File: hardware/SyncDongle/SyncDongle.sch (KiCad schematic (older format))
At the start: 3 parts

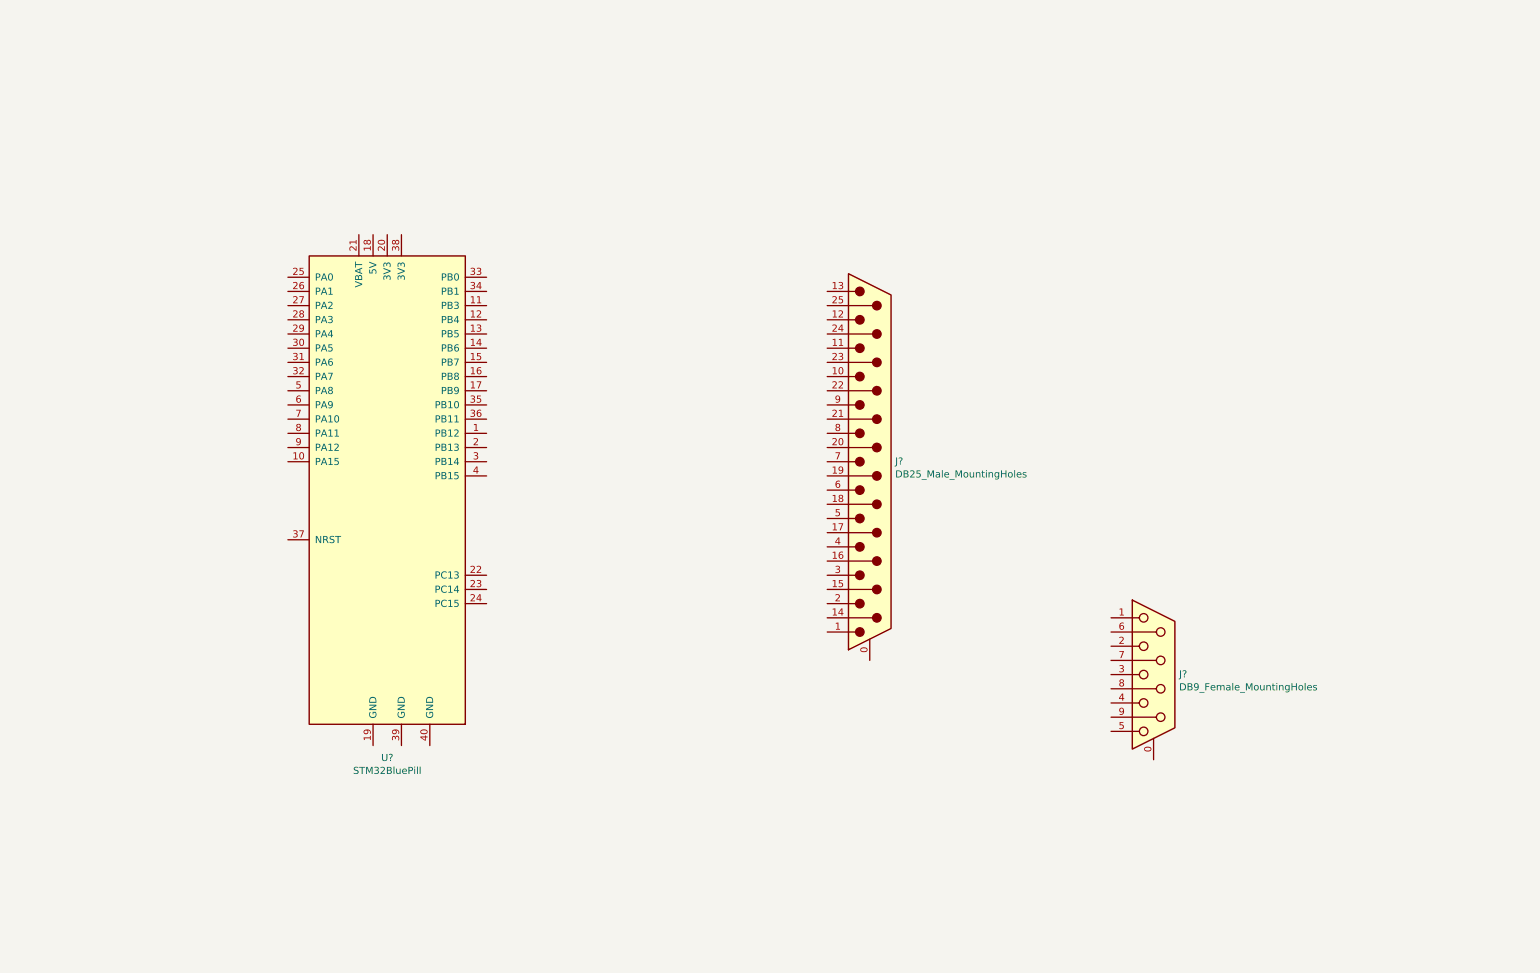
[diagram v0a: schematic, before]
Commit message: Added MAX208
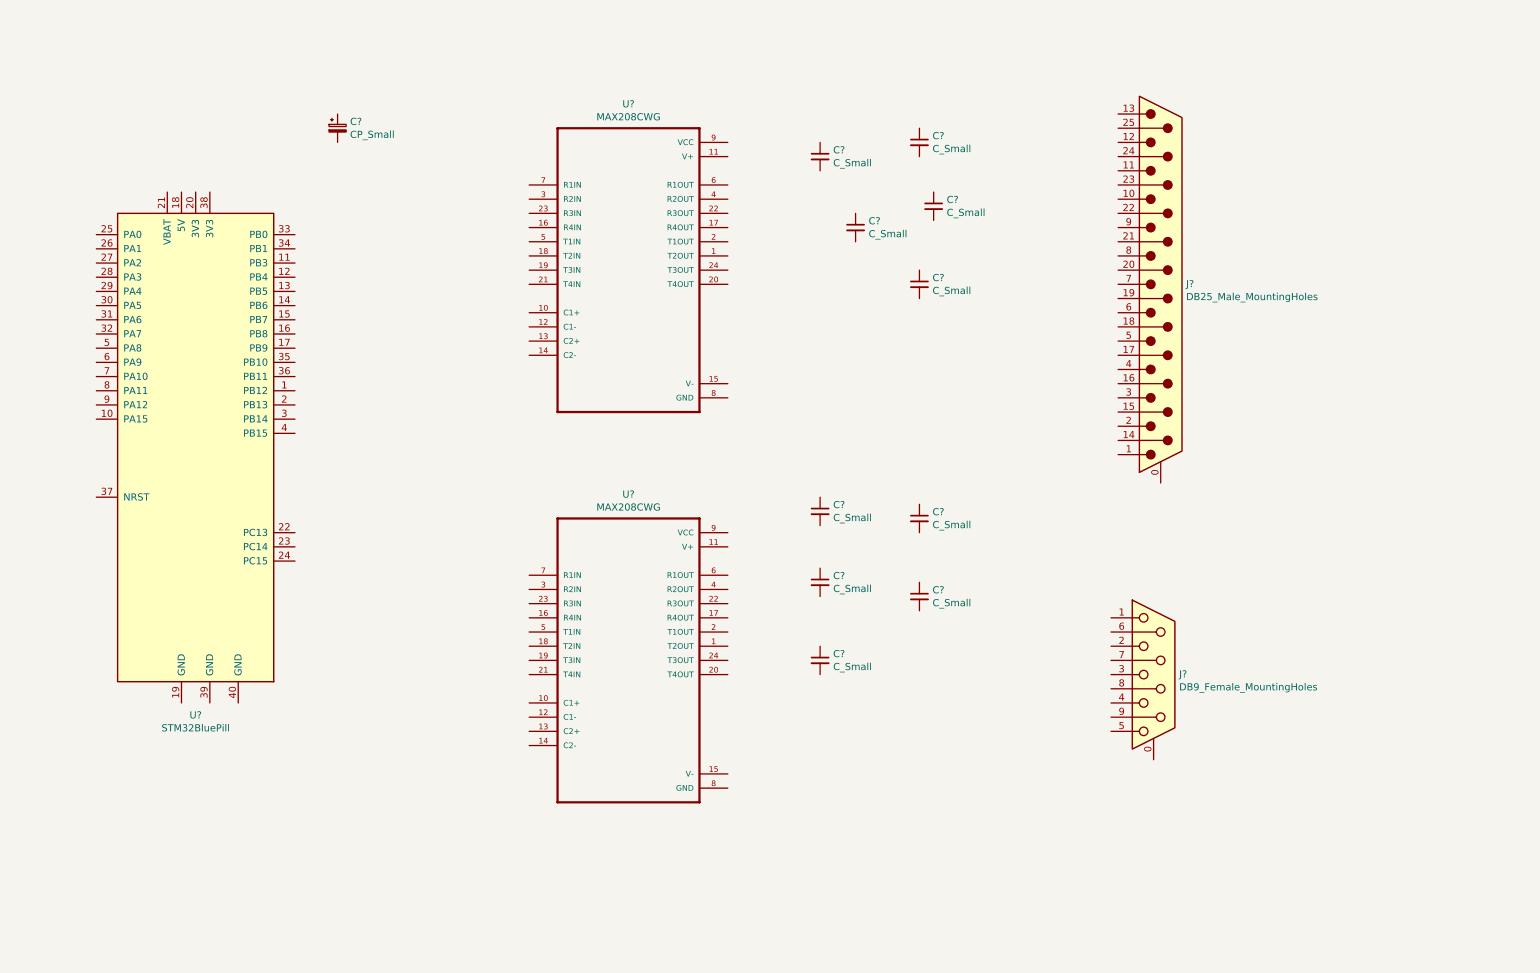
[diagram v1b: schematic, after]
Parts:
- added C? (x10): C_Small, symbol Device:C_Small
- added C?: CP_Small, symbol Device:CP_Small
- added U? (x2): MAX208CWG, SOIC127P1032X265-24N, symbol MAX208CWG:MAX208CWG
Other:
- moved on the sheet: J?, U?
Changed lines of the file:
@@
 EESchema Schematic File Version 4
+LIBS:SyncDongle-cache
 EELAYER 26 0
 EELAYER END
@@
 L MyLibrary:STM32BluePill U?
 U 1 1 5F1ADFA5
-P 3850 4050
-F 0 "U?" H 3850 2164 50  0000 C CNN
-F 1 "STM32BluePill" H 3850 2073 50  0000 C CNN
-F 2 "Housings_DIP:DIP-40_W15.24mm" H 3900 4150 50  0001 C CIN
-F 3 "" H 3850 4100 50  0001 C CNN
-	1    3850 4050
+P 2500 3750
+F 0 "U?" H 2500 1864 50  0000 C CNN
+F 1 "STM32BluePill" H 2500 1773 50  0000 C CNN
+F 2 "Housings_DIP:DIP-40_W15.24mm" H 2550 3850 50  0001 C CIN
+F 3 "" H 2500 3800 50  0001 C CNN
+	1    2500 3750
 	1    0    0    -1
 $EndComp
@@
 L Connector:DB25_Male_MountingHoles J?
 U 1 1 5F1AE32F
-P 7250 3850
-F 0 "J?" H 7429 3853 50  0000 L CNN
-F 1 "DB25_Male_MountingHoles" H 7429 3762 50  0000 L CNN
-F 2 "" H 7250 3850 50  0001 C CNN
-F 3 " ~" H 7250 3850 50  0001 C CNN
-	1    7250 3850
+P 9300 2600
+F 0 "J?" H 9479 2603 50  0000 L CNN
+F 1 "DB25_Male_MountingHoles" H 9479 2512 50  0000 L CNN
+F 2 "" H 9300 2600 50  0001 C CNN
+F 3 " ~" H 9300 2600 50  0001 C CNN
+	1    9300 2600
 	1    0    0    -1
 $EndComp
@@
 	1    0    0    -1
 $EndComp
+$Comp
+L MAX208CWG:MAX208CWG U?
+U 1 1 5F185462
+P 5550 2500
+F 0 "U?" H 5550 3670 50  0000 C CNN
+F 1 "MAX208CWG" H 5550 3579 50  0000 C CNN
+F 2 "SOIC127P1032X265-24N" H 5550 2500 50  0001 L BNN
+F 3 "SOIC-24 Maxim" H 5550 2500 50  0001 L BNN
+F 4 "Maxim Integrated" H 5550 2500 50  0001 L BNN "Field4"
+F 5 "MAX208CWG+" H 5550 2500 50  0001 L BNN "Field5"
+F 6 "https://snapeda.com/shop?store=DigiKey&id=128491" H 5550 2500 50  0001 L BNN "Field6"
+F 7 "4/4 Transceiver Full RS232 24-SOIC" H 5550 2500 50  0001 L BNN "Field7"
+F 8 "MAX208CWG+TTR-ND" H 5550 2500 50  0001 L BNN "Field8"
+F 9 "https://snapeda.com/shop?store=Mouser&id=128491" H 5550 2500 50  0001 L BNN "Field9"
+	1    5550 2500
+	1    0    0    -1
+$EndComp
+$Comp
+L MAX208CWG:MAX208CWG U?
+U 1 1 5F185592
+P 5550 5250
+F 0 "U?" H 5550 6420 50  0000 C CNN
+F 1 "MAX208CWG" H 5550 6329 50  0000 C CNN
+F 2 "SOIC127P1032X265-24N" H 5550 5250 50  0001 L BNN
+F 3 "SOIC-24 Maxim" H 5550 5250 50  0001 L BNN
+F 4 "Maxim Integrated" H 5550 5250 50  0001 L BNN "Field4"
+F 5 "MAX208CWG+" H 5550 5250 50  0001 L BNN "Field5"
+F 6 "https://snapeda.com/shop?store=DigiKey&id=128491" H 5550 5250 50  0001 L BNN "Field6"
+F 7 "4/4 Transceiver Full RS232 24-SOIC" H 5550 5250 50  0001 L BNN "Field7"
+F 8 "MAX208CWG+TTR-ND" H 5550 5250 50  0001 L BNN "Field8"
+F 9 "https://snapeda.com/shop?store=Mouser&id=128491" H 5550 5250 50  0001 L BNN "Field9"
+	1    5550 5250
+	1    0    0    -1
+$EndComp
+$Comp
+L Device:C_Small C?
+U 1 1 5F185808
+P 6900 1700
+F 0 "C?" H 6992 1746 50  0000 L CNN
+F 1 "C_Small" H 6992 1655 50  0000 L CNN
+F 2 "" H 6900 1700 50  0001 C CNN
+F 3 "~" H 6900 1700 50  0001 C CNN
+	1    6900 1700
+	1    0    0    -1
+$EndComp
+$Comp
+L Device:C_Small C?
+U 1 1 5F185866
+P 7600 1600
+F 0 "C?" H 7692 1646 50  0000 L CNN
+F 1 "C_Small" H 7692 1555 50  0000 L CNN
+F 2 "" H 7600 1600 50  0001 C CNN
+F 3 "~" H 7600 1600 50  0001 C CNN
+	1    7600 1600
+	1    0    0    -1
+$EndComp
+$Comp
+L Device:C_Small C?
+U 1 1 5F1858C6
+P 7700 2050
+F 0 "C?" H 7792 2096 50  0000 L CNN
+F 1 "C_Small" H 7792 2005 50  0000 L CNN
+F 2 "" H 7700 2050 50  0001 C CNN
+F 3 "~" H 7700 2050 50  0001 C CNN
+	1    7700 2050
+	1    0    0    -1
+$EndComp
+$Comp
+L Device:C_Small C?
+U 1 1 5F1858FA
+P 7150 2200
+F 0 "C?" H 7242 2246 50  0000 L CNN
+F 1 "C_Small" H 7242 2155 50  0000 L CNN
+F 2 "" H 7150 2200 50  0001 C CNN
+F 3 "~" H 7150 2200 50  0001 C CNN
+	1    7150 2200
+	1    0    0    -1
+$EndComp
+$Comp
+L Device:C_Small C?
+U 1 1 5F185938
+P 7600 2600
+F 0 "C?" H 7692 2646 50  0000 L CNN
+F 1 "C_Small" H 7692 2555 50  0000 L CNN
+F 2 "" H 7600 2600 50  0001 C CNN
+F 3 "~" H 7600 2600 50  0001 C CNN
+	1    7600 2600
+	1    0    0    -1
+$EndComp
+$Comp
+L Device:C_Small C?
+U 1 1 5F185976
+P 6900 4200
+F 0 "C?" H 6992 4246 50  0000 L CNN
+F 1 "C_Small" H 6992 4155 50  0000 L CNN
+F 2 "" H 6900 4200 50  0001 C CNN
+F 3 "~" H 6900 4200 50  0001 C CNN
+	1    6900 4200
+	1    0    0    -1
+$EndComp
+$Comp
+L Device:C_Small C?
+U 1 1 5F1859D8
+P 7600 4250
+F 0 "C?" H 7692 4296 50  0000 L CNN
+F 1 "C_Small" H 7692 4205 50  0000 L CNN
+F 2 "" H 7600 4250 50  0001 C CNN
+F 3 "~" H 7600 4250 50  0001 C CNN
+	1    7600 4250
+	1    0    0    -1
+$EndComp
+$Comp
+L Device:C_Small C?
+U 1 1 5F185A1C
+P 6900 4700
+F 0 "C?" H 6992 4746 50  0000 L CNN
+F 1 "C_Small" H 6992 4655 50  0000 L CNN
+F 2 "" H 6900 4700 50  0001 C CNN
+F 3 "~" H 6900 4700 50  0001 C CNN
+	1    6900 4700
+	1    0    0    -1
+$EndComp
+$Comp
+L Device:C_Small C?
+U 1 1 5F185A5C
+P 7600 4800
+F 0 "C?" H 7692 4846 50  0000 L CNN
+F 1 "C_Small" H 7692 4755 50  0000 L CNN
+F 2 "" H 7600 4800 50  0001 C CNN
+F 3 "~" H 7600 4800 50  0001 C CNN
+	1    7600 4800
+	1    0    0    -1
+$EndComp
+$Comp
+L Device:C_Small C?
+U 1 1 5F185AA2
+P 6900 5250
+F 0 "C?" H 6992 5296 50  0000 L CNN
+F 1 "C_Small" H 6992 5205 50  0000 L CNN
+F 2 "" H 6900 5250 50  0001 C CNN
+F 3 "~" H 6900 5250 50  0001 C CNN
+	1    6900 5250
+	1    0    0    -1
+$EndComp
+$Comp
+L Device:CP_Small C?
+U 1 1 5F185B27
+P 3500 1500
+F 0 "C?" H 3588 1546 50  0000 L CNN
+F 1 "CP_Small" H 3588 1455 50  0000 L CNN
+F 2 "" H 3500 1500 50  0001 C CNN
+F 3 "~" H 3500 1500 50  0001 C CNN
+	1    3500 1500
+	1    0    0    -1
+$EndComp

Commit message: Schematic almost ready.
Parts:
- removed C? (x5): C_Small, symbol Device:C_Small
- removed U?: MAX208CWG, SOIC127P1032X265-24N, symbol MAX208CWG:MAX208CWG
- added C10, C11, C4, C5, C9: 0.1u, symbol Device:C_Small
- added SW1: SW_DIP_x09, symbol Switch:SW_DIP_x09
- added U3: MAX208CWG, SOIC127P1032X265-24N, symbol MAX208CWG:MAX208CWG
- C1: renamed from C?; value CP_Small -> 10u
- C2, C3, C6, C7, C8: renamed from C?; value C_Small -> 0.1u
- gave numbers to parts that had none: 4
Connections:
- net labels added: +5V, CMOS_CKIN, CMOS_CKOUT, CMOS_CTS, CMOS_DCD, CMOS_DSR, CMOS_DTR, CMOS_D_RX, CMOS_D_TX, CMOS_RD, CMOS_RTS, CMOS_TD, EIA_CLK15, EIA_CLK17, EIA_CLK24, EIA_CLKIN, EIA_CTS, EIA_DCD, EIA_DSR, EIA_DTR, EIA_D_RX, EIA_D_TX, EIA_RD, EIA_RTS, EIA_TD, GND
- wire segments 0 -> 143
- no-connect marks 0 -> 51
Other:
- moved on the sheet: C1, C2, C3, C6, C7, C8, J1, J2, U2

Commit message: Fixed layout.
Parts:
- removed SW1: SW_DIP_x09, symbol Switch:SW_DIP_x09
- added SW1: SW_DIP_x10, Package_DIP:DIP-20_W7.62mm_LongPads, symbol Switch:SW_DIP_x10
- C1: footprint (none) -> Capacitor_THT:CP_Radial_D5.0mm_P2.00mm
- U2, U3: footprint SOIC127P1032X265-24N -> Package_DIP:DIP-24_W7.62mm_LongPads
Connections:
- net labels added: CMOS_RI, EIA_CLKOUT, EIA_RI
- net labels removed: EIA_CLK15, EIA_CLK17, EIA_CLK24
- wire segments 143 -> 150
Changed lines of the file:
@@
 F 0 "U2" H 5300 7220 50  0000 C CNN
 F 1 "MAX208CWG" H 5300 7129 50  0000 C CNN
-F 2 "SOIC127P1032X265-24N" H 5300 6050 50  0001 L BNN
+F 2 "Package_DIP:DIP-24_W7.62mm_LongPads" H 5300 6050 50  0001 L BNN
 F 3 "SOIC-24 Maxim" H 5300 6050 50  0001 L BNN
 F 4 "Maxim Integrated" H 5300 6050 50  0001 L BNN "Field4"
@@
 F 0 "C1" H 2738 1646 50  0000 L CNN
 F 1 "10u" H 2738 1555 50  0000 L CNN
-F 2 "" H 2650 1600 50  0001 C CNN
+F 2 "Capacitor_THT:CP_Radial_D5.0mm_P2.00mm" H 2650 1600 50  0001 C CNN
 F 3 "~" H 2650 1600 50  0001 C CNN
 	1    2650 1600
@@
 Text Label 4150 5850 0    50   ~ 0
 CMOS_D_TX
-Wire Wire Line
-	4600 5950 4500 5950
-Wire Wire Line
-	4600 6050 4500 6050
-Wire Wire Line
-	4600 6150 4500 6150
 Text Label 3600 6150 0    50   ~ 0
 CMOS_CKOUT
@@
 EIA_D_TX
 Wire Wire Line
-	6000 5950 6400 5950
-Text Label 6050 5950 0    50   ~ 0
-EIA_CLK24
-Wire Wire Line
 	6000 6050 6400 6050
-Text Label 6050 6050 0    50   ~ 0
-EIA_CLK17
 Wire Wire Line
 	6000 6150 6400 6150
 Text Label 6050 6150 0    50   ~ 0
-EIA_CLK15
+EIA_CLKOUT
 $Comp
 L power:GND #PWR05
@@
 Wire Wire Line
 	10250 3350 9750 3350
-$Comp
-L Switch:SW_DIP_x09 SW1
-U 1 1 5F1A85E1
-P 8550 2550
-F 0 "SW1" H 8550 3217 50  0000 C CNN
-F 1 "SW_DIP_x09" H 8550 3126 50  0000 C CNN
-F 2 "" H 8550 2550 50  0001 C CNN
-F 3 "" H 8550 2550 50  0001 C CNN
-	1    8550 2550
-	1    0    0    -1
-$EndComp
-Wire Wire Line
-	8850 2150 10250 2150
-Wire Wire Line
-	8850 2550 10250 2550
 Wire Wire Line
 	8850 2850 9100 2850
@@
 	10250 1450 9300 1450
 Wire Wire Line
-	9300 1450 9300 2250
-Wire Wire Line
-	9300 2250 9050 2250
-Wire Wire Line
-	8850 2350 9050 2350
-Wire Wire Line
-	9050 2350 9050 2250
-Connection ~ 9050 2250
-Wire Wire Line
-	9050 2250 8850 2250
-Wire Wire Line
-	8850 2450 9250 2450
-Wire Wire Line
-	9250 2450 9250 2750
+	9300 1450 9300 2050
+Wire Wire Line
+	9300 2050 9050 2050
+Wire Wire Line
+	8850 2150 9050 2150
+Wire Wire Line
+	9050 2150 9050 2050
+Connection ~ 9050 2050
+Wire Wire Line
+	9050 2050 8850 2050
+Wire Wire Line
+	8850 2550 9250 2550
+Wire Wire Line
+	9250 2550 9250 2750
 Wire Wire Line
 	9250 2750 10250 2750
 Wire Wire Line
-	8250 2150 7800 2150
-Wire Wire Line
-	8250 2250 8200 2250
-Wire Wire Line
-	8250 2350 7800 2350
-Wire Wire Line
-	8250 2450 7800 2450
-Wire Wire Line
-	8250 2550 7800 2550
+	8250 2450 7700 2450
+Wire Wire Line
+	8250 2550 7700 2550
 Wire Wire Line
 	8250 2650 8200 2650
@@
 	8250 2750 8200 2750
 Wire Wire Line
-	8250 2850 7800 2850
-Wire Wire Line
-	8250 2950 7800 2950
+	8250 2850 8150 2850
+Wire Wire Line
+	8250 2950 8150 2950
 $Comp
 L power:GND #PWR010
@@
 F 0 "U3" H 5650 3470 50  0000 C CNN
 F 1 "MAX208CWG" H 5650 3379 50  0000 C CNN
-F 2 "SOIC127P1032X265-24N" H 5650 2300 50  0001 L BNN
+F 2 "Package_DIP:DIP-24_W7.62mm_LongPads" H 5650 2300 50  0001 L BNN
 F 3 "SOIC-24 Maxim" H 5650 2300 50  0001 L BNN
 F 4 "Maxim Integrated" H 5650 2300 50  0001 L BNN "Field4"
@@
 Text Label 6400 2000 0    50   ~ 0
 CMOS_CKIN
-Wire Wire Line
-	4500 6050 4500 6150
-Connection ~ 4500 6150
-Wire Wire Line
-	4500 6150 3600 6150
-Wire Wire Line
-	4500 5950 4500 6050
-Connection ~ 4500 6050
-Text Label 7800 2950 0    50   ~ 0
-EIA_CLK15
-Text Label 7800 2850 0    50   ~ 0
-EIA_CLK17
-Text Label 7800 2350 0    50   ~ 0
-EIA_CLK24
+Text Label 7700 2150 0    50   ~ 0
+EIA_CLKOUT
 Wire Wire Line
 	8200 2750 8200 2650
-Connection ~ 8200 2250
-Wire Wire Line
-	8200 2250 7800 2250
-Connection ~ 8200 2650
-Wire Wire Line
-	8200 2650 8200 2250
-Text Label 7800 2250 0    50   ~ 0
+Text Label 7700 2050 0    50   ~ 0
 EIA_CLKIN
-Text Label 7800 2150 0    50   ~ 0
+Text Label 7700 2350 0    50   ~ 0
 EIA_DCD
-Text Label 7800 2450 0    50   ~ 0
+Text Label 7700 2550 0    50   ~ 0
 EIA_CTS
-Text Label 7800 2550 0    50   ~ 0
+Text Label 7700 2450 0    50   ~ 0
 EIA_DSR
 Text Label 9750 3350 0    50   ~ 0
@@
 NoConn ~ 10250 2050
 NoConn ~ 10250 1950
-NoConn ~ 10250 1850
 NoConn ~ 10250 1750
 NoConn ~ 10250 1650
@@
 NoConn ~ 3200 3150
 NoConn ~ 3200 2650
-NoConn ~ 3200 2450
 NoConn ~ 3200 2350
 NoConn ~ 3200 2250
@@
 	3200 1750 2650 1750
 Connection ~ 2650 1750
+$Comp
+L Switch:SW_DIP_x10 SW1
+U 1 1 5F1A6837
+P 8550 2550
+F 0 "SW1" H 8550 3317 50  0000 C CNN
+F 1 "SW_DIP_x10" H 8550 3226 50  0000 C CNN
+F 2 "Package_DIP:DIP-20_W7.62mm_LongPads" H 8550 2550 50  0001 C CNN
+F 3 "" H 8550 2550 50  0001 C CNN
+	1    8550 2550
+	1    0    0    -1
+$EndComp
+Wire Wire Line
+	10250 1850 9350 1850
+Wire Wire Line
+	9350 1850 9350 2250
+Wire Wire Line
+	9350 2250 8850 2250
+Wire Wire Line
+	9450 2150 9450 2350
+Wire Wire Line
+	9450 2350 8850 2350
+Wire Wire Line
+	9450 2150 10250 2150
+Wire Wire Line
+	8150 2950 8150 2850
+Wire Wire Line
+	8200 2650 8200 2050
+Wire Wire Line
+	8200 2050 8250 2050
+Connection ~ 8200 2650
+Wire Wire Line
+	8200 2050 7700 2050
+Connection ~ 8200 2050
+Wire Wire Line
+	8250 2250 7700 2250
+Wire Wire Line
+	7700 2350 8250 2350
+Wire Wire Line
+	7700 2150 8150 2150
+Wire Wire Line
+	8150 2850 8150 2150
+Connection ~ 8150 2850
+Connection ~ 8150 2150
+Wire Wire Line
+	8150 2150 8250 2150
+Text Label 7700 2250 0    50   ~ 0
+EIA_RI
+Wire Wire Line
+	10250 2550 9350 2550
+Wire Wire Line
+	9350 2550 9350 2450
+Wire Wire Line
+	9350 2450 8850 2450
+Wire Wire Line
+	3600 6150 4600 6150
+Wire Wire Line
+	4600 6050 4150 6050
+Text Label 4150 6050 0    50   ~ 0
+CMOS_RI
+Text Label 6050 6050 0    50   ~ 0
+EIA_RI
+NoConn ~ 6000 5950
+NoConn ~ 4600 5950
+Wire Wire Line
+	3200 2450 3650 2450
+Text Label 3250 2450 0    50   ~ 0
+CMOS_RI
 $EndSCHEMATC
